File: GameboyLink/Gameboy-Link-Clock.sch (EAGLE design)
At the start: 38 parts, among them IC1 MEGA8-AI, J1 AVR_SPI_PRG_6PTH, Q1 16MHz, U1 DS1307Z, Y1 32.768kHz

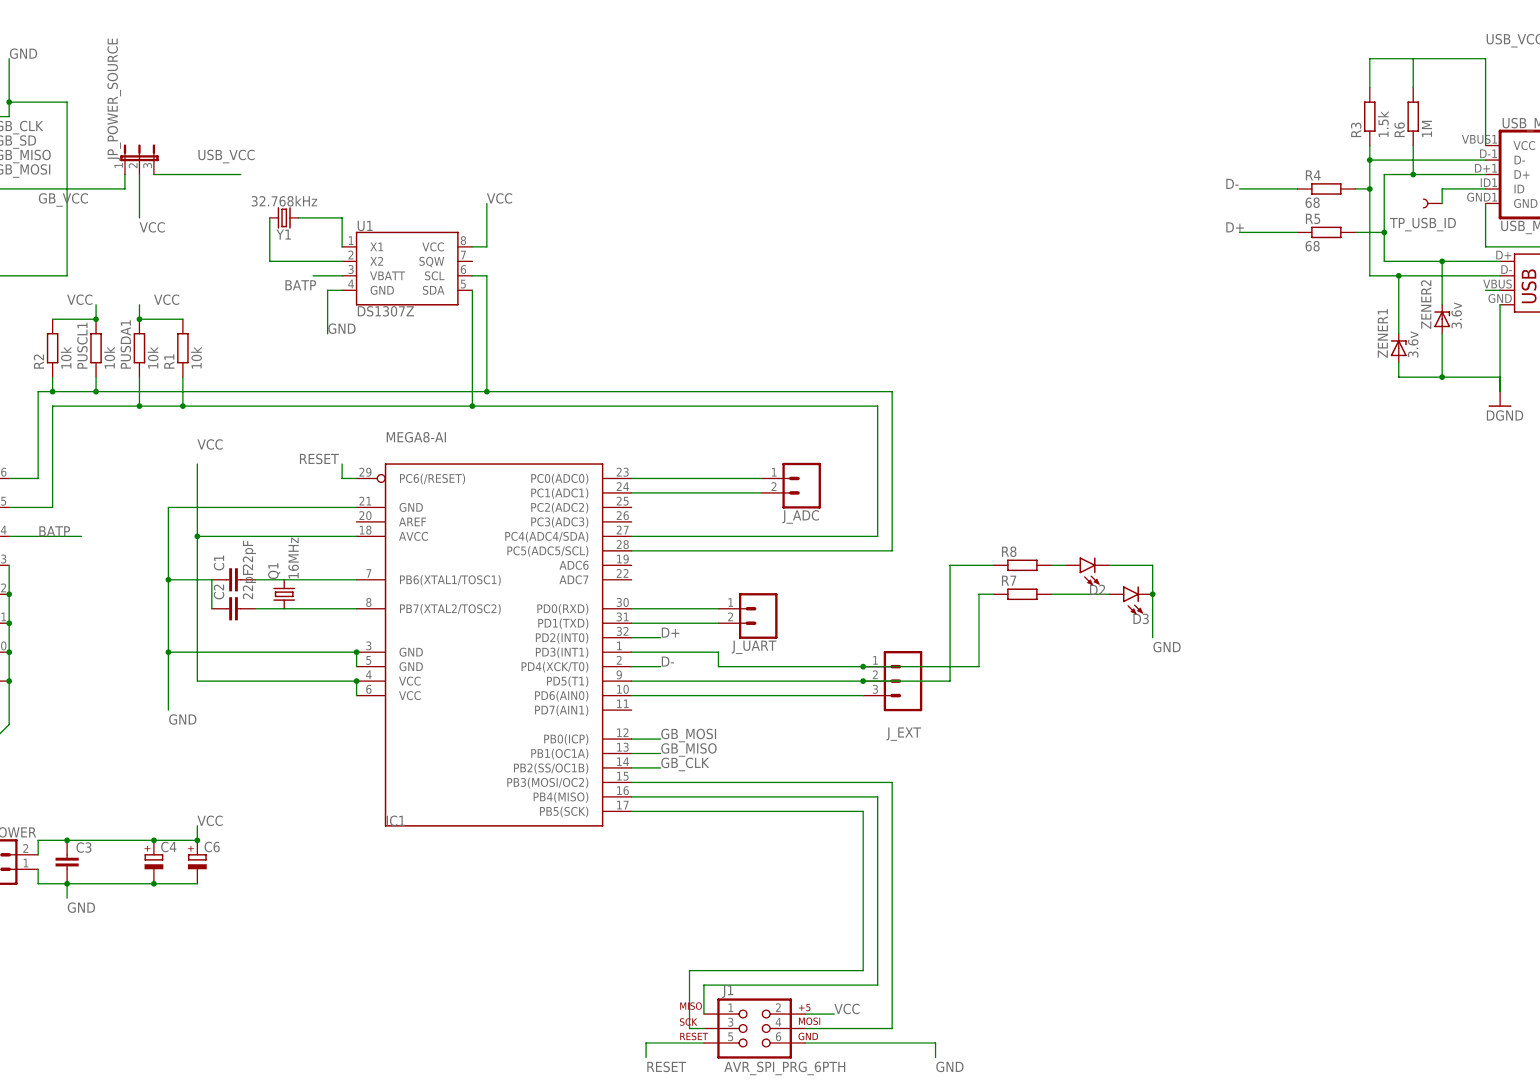
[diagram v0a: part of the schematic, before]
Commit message: Overall layout ok first pass, now cosmetics
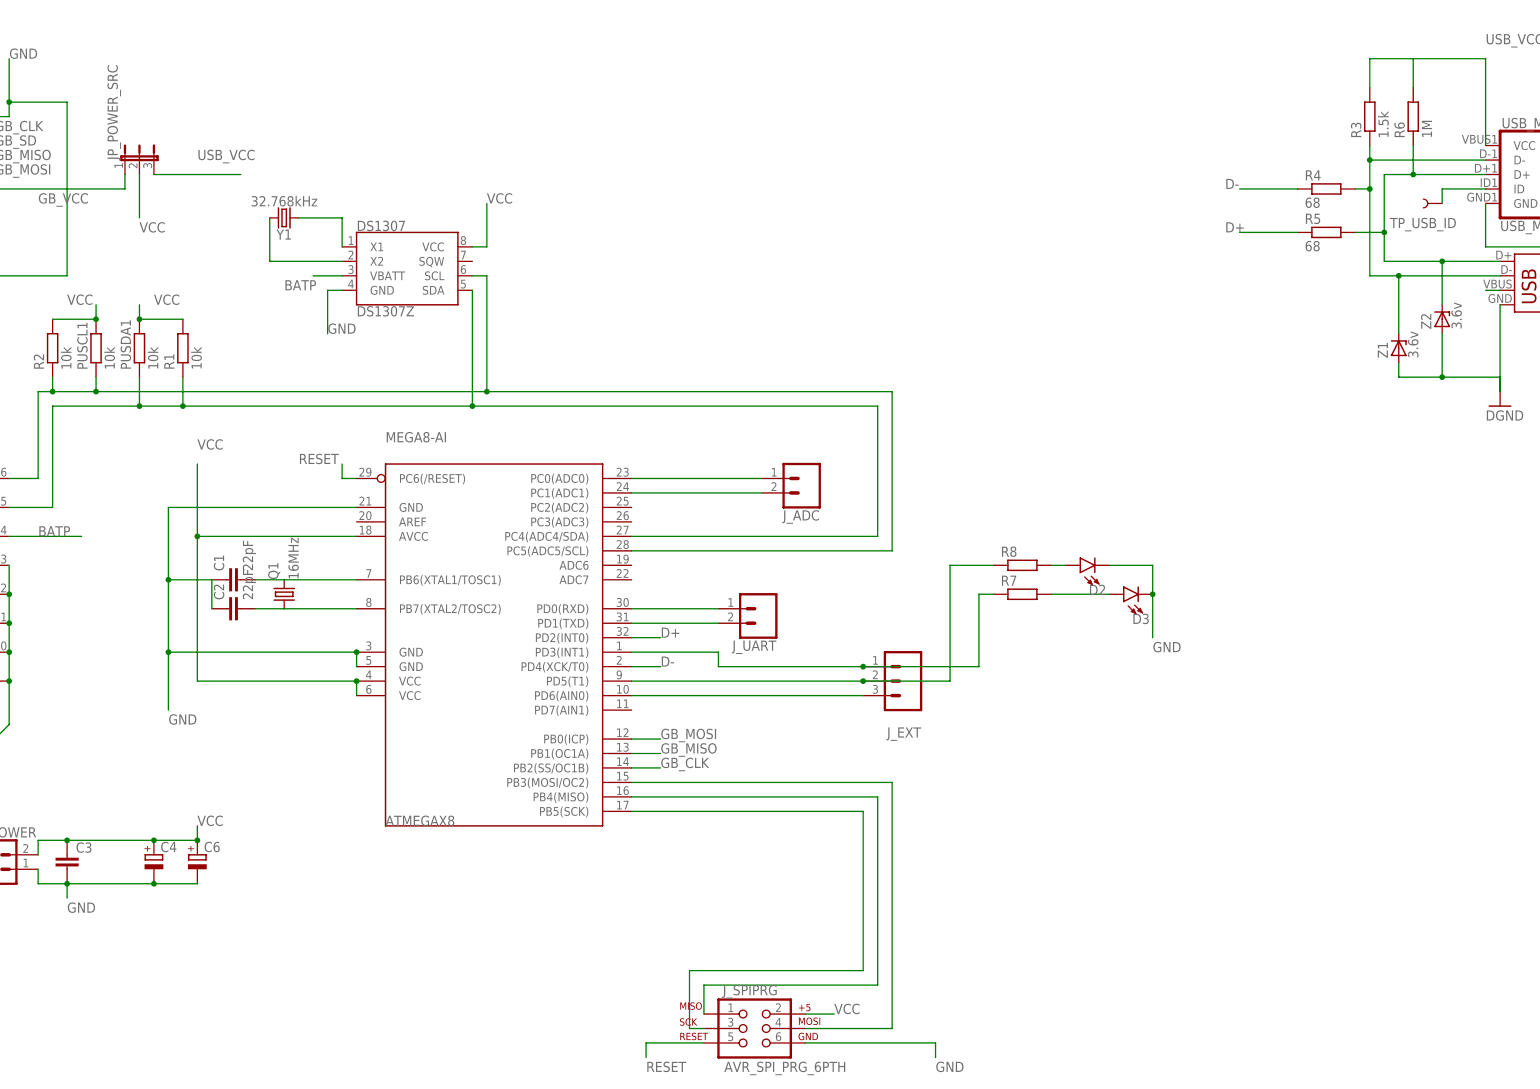
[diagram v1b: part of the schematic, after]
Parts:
- renumbered IC1 to ATMEGAX8, J1 to J_SPIPRG, JP_POWER_SOURCE to JP_POWER_SRC, U$2 to DS3231, U1 to DS1307, ZENER1 to Z1, ZENER2 to Z2
